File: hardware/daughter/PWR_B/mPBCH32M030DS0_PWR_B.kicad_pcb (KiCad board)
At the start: 2 copper layers, 66 x 66 mm, 76 parts, among them J1 B2B_PWR, J2 OUT0, J3 B2B_SIG, J4 OUT1, J5 OUT2, J6 OUT3, Q1 TKR74F04PB, Q2 TKR74F04PB, Q3 TKR74F04PB, Q4 TKR74F04PB, Q5 TKR74F04PB, Q6 TKR74F04PB, Q7 TKR74F04PB, Q8 TKR74F04PB

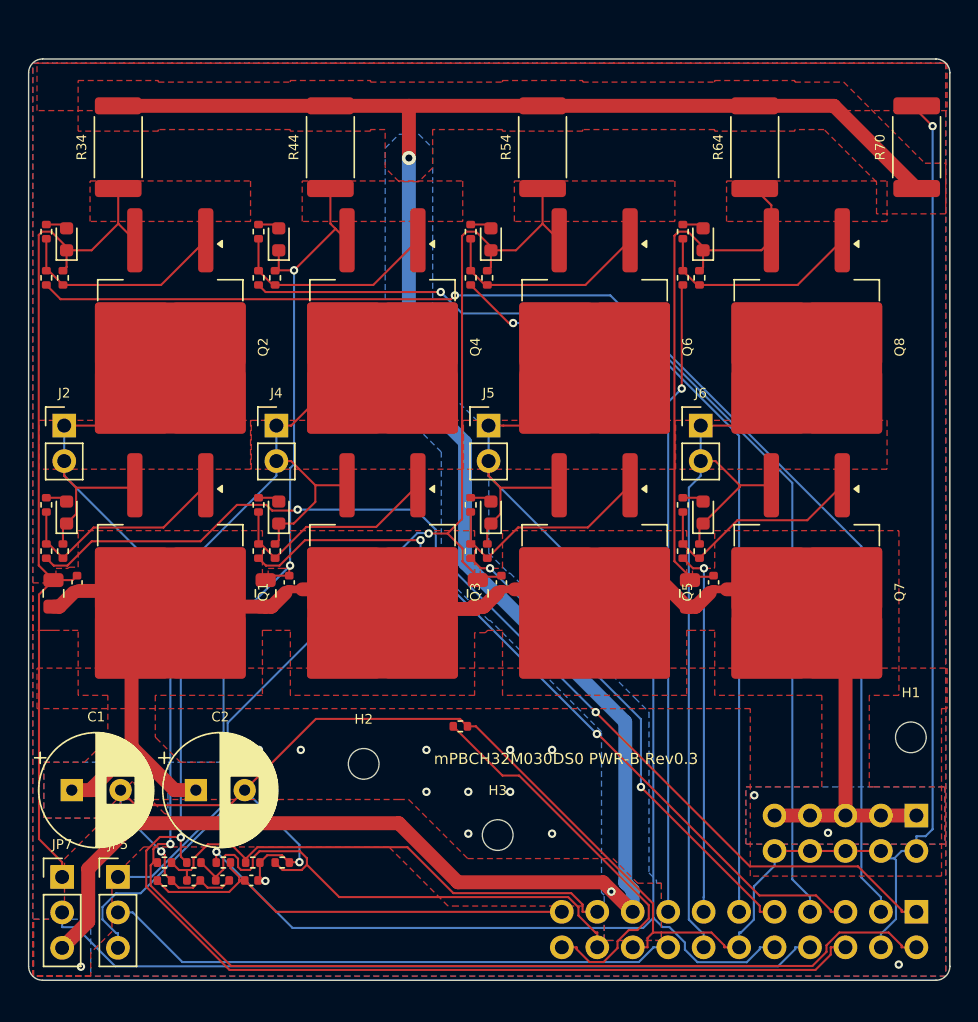
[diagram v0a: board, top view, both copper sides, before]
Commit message: Rev 0.4: DIP-42 MCU module + power boards A/B/C (KiCad 8)
- MCU module: 20.32 x 53.34mm (8 x 21 grid), DIP-42 (0.6in rows), fits
  an 82 x 52mm breadboard. Headers can be fitted from either side;
  signal names on bottom silk. All LEDs (power, status, 8 gate LEDs) on
  the module top.
- Power boards take the module in two 1x21 sockets (left/right
  symmetric mating). FETs/shunts on the heatsink side, no LEDs.
  Voltage-dependent parts (TVS, OVP divider, bulk caps, BEMF divider)
  moved to the power boards. Breakout board D removed.
  A/C: 20.32 x 71.94mm, B (TO-263 x8): 40.64 x 66.94mm.
- Capacitors re-selected for realistic size vs voltage/capacitance
  (4.7uF 1608, 10uF/25V 2012, 10uF/50V 1206, 4.7nF/100V 1608, low
  profile electrolytics).
- Schematics and boards generated in KiCad 8 format; netlists verified
  with KiCad 8.0.9.
- Layout pipeline: Freerouting bridge (parallel), second pass, early
  repair before pours, island-aware maze repair, DRC via kicad-cli.
- DRC: power boards A/B/C have 0 unconnected / 0 electrical errors.
  The MCU module still has unrouted connections (work in progress).

Co-Authored-By: Claude Opus 5.5 <noreply@anthropic.com>
Claude-Session: https://claude.ai/code/session_01LENFjjhDfYjJZV1NWhB9uV
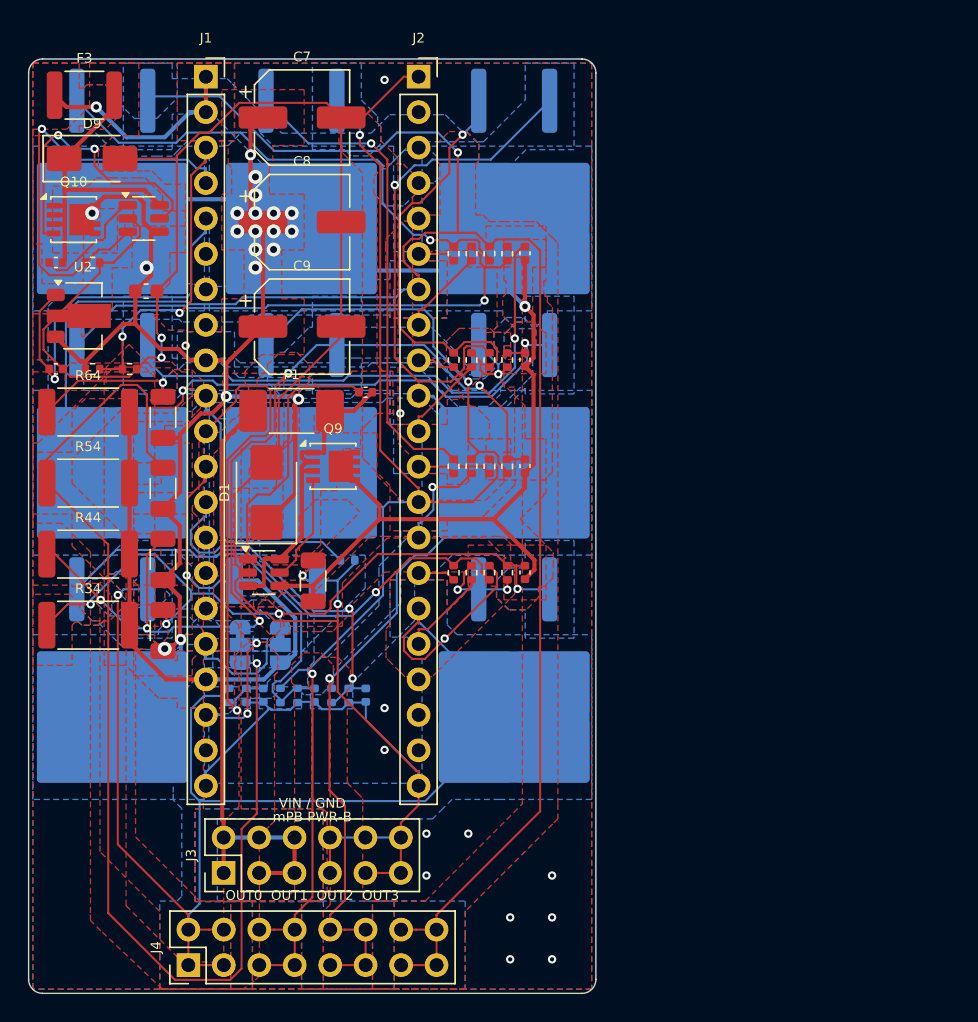
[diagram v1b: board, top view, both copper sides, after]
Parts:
- removed C2: 330uF/35V, CP_Radial_D8.0mm_P3.50mm
- removed D10: RED GH0, LED_0603_1608Metric
- removed D11: GREEN GL0, LED_0603_1608Metric
- removed D12: RED GH1, LED_0603_1608Metric
- removed D13: GREEN GL1, LED_0603_1608Metric
- removed D14: RED GH2, LED_0603_1608Metric
- removed D15: GREEN GL2, LED_0603_1608Metric
- removed D16: RED GH3, LED_0603_1608Metric
- removed D17: GREEN GL3, LED_0603_1608Metric
- removed H1, H2, H3: M2, MountingHole_2.2mm_M2
- removed J5: OUT2, PinHeader_1x02_P2.54mm_Vertical
- removed J6: OUT3, PinHeader_1x02_P2.54mm_Vertical
- removed R35, R36, R45, R46, R55, R56, R65, R66: 22k, R_0402_1005Metric
- added C3: 1uF/50V, C_0603_1608Metric, F.Cu at (8.41, 16.6)
- added C4: 1uF/25V, C_0402_1005Metric, F.Cu at (1.96, 22.2)
- added C5: 0.1uF/50V, C_0402_1005Metric, F.Cu at (24.1, 23.9)
- added C6: 0.1uF/50V, C_0402_1005Metric, F.Cu at (1.96, 14.6)
- added C7: 47uF/35V, CP_Elec_6.3x5.9, F.Cu at (19.6, 4.20)
- added C8: 47uF/35V, CP_Elec_6.3x5.9, F.Cu at (19.6, 11.7)
- added C9: 47uF/35V, CP_Elec_6.3x5.9, F.Cu at (19.6, 19.2)
- added D1: SMBJ24A, D_SMB, F.Cu at (17.0, 31.1)
- added D9: SMAJ20A, D_SMA, F.Cu at (4.54, 7.13)
- added F1: 10A, Fuse_Littelfuse_NANO2_2410, F.Cu at (18.8, 25.2)
- added F3: 5A, Fuse_1812_4532Metric, F.Cu at (4.00, 2.60)
- added Q10: TPN1R603PL, Vishay_PowerPAK_1212-8_Single, F.Cu at (3.23, 11.5)
- added Q9: TPN2R304PL, Vishay_PowerPAK_1212-8_Single, F.Cu at (21.8, 29.2)
- added R11: 180k 1%, R_0402_1005Metric, F.Cu at (4.58, 22.2)
- added R12: 10k 1%, R_0402_1005Metric, F.Cu at (7.23, 22.2)
- added R6: 100k, R_0402_1005Metric, F.Cu at (4.58, 14.6)
- added U2: 78L05, SOT-89-3, F.Cu at (3.90, 18.4)
- added U4: LM74700-Q1, SOT-23-6, F.Cu at (16.8, 36.8)
- added U5: LM74700-Q1, SOT-23-6, F.Cu at (8.24, 11.4)
- C1: value 330uF/35V -> 10uF/50V; footprint CP_Radial_D8.0mm_P3.50mm -> C_1206_3216Metric
- C31, C41, C51, C61: footprint C_0805_2012Metric -> C_1206_3216Metric
- C71, C72, C73, Q1, Q2, Q3, Q4, Q5, Q6, Q7, Q8, R70, R71, R72, R74, R75, R77, R78, TH1: moved to B.Cu
- J1: value B2B_PWR -> SOCK_L; footprint PinSocket_2x05_P2.54mm_Vertical -> PinSocket_1x21_P2.54mm_Vertical; moved to F.Cu
- J2: value OUT0 -> SOCK_R; footprint PinHeader_1x02_P2.54mm_Vertical -> PinSocket_1x21_P2.54mm_Vertical
- J3: value B2B_SIG -> PWR_IN; footprint PinSocket_2x11_P2.54mm_Vertical -> PinHeader_2x06_P2.54mm_Vertical; moved to F.Cu
- J4: value OUT1 -> MOTOR; footprint PinHeader_1x02_P2.54mm_Vertical -> PinHeader_2x08_P2.54mm_Vertical
- JP5, JP7: footprint PinHeader_1x03_P2.54mm_Vertical -> SolderJumper-3_P1.3mm_Bridged12_RoundedPad1.0x1.5mm_NumberLabels; moved to B.Cu
- moved J1 73.4 mm to (12.7, 1.27), turned to 0 degrees
- moved Q7 56.9 mm to (6.00, 10.6)
- moved R70 55.4 mm to (17.7, 37.4), turned to 0 degrees
- moved R64 51.4 mm to (4.26, 25.3), turned to 0 degrees
- moved Q8 50.3 mm to (6.00, 28.1)
- moved J3 49.7 mm to (14.0, 58.3)
- moved R54 40.5 mm to (4.26, 30.4), turned to 0 degrees
- moved C61 39.8 mm to (9.62, 25.7)
- moved J4 39.2 mm to (11.4, 64.9), turned to 90 degrees
- moved R33 38.2 mm to (34.3, 36.8)
- moved R32 37.1 mm to (31.7, 36.8)
- moved J2 35.6 mm to (27.9, 1.27)
- moved Q2 35.1 mm to (34.8, 45.6)
- moved R34 34.3 mm to (4.26, 40.6), turned to 0 degrees
- moved R44 33.9 mm to (4.26, 35.5), turned to 0 degrees
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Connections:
- J1 pad 1: VBUS -> USB_VBUS
- J1 pad 10: GND -> NTC
- J1 pad 2: GND -> USB_VBUS
- J1 pad 3: VBUS -> VBUS_SNS
- J1 pad 4: GND -> PD_PWR_EN
- J1 pad 5: VBUS -> +5V
- J1 pad 6: GND -> +3V3
- J1 pad 7: VBUS -> SWDIO
- J1 pad 8: GND -> nRST
- J2 pad 1: SW0 -> GND
- J2 pad 2: SW0 -> UART_TX
- J3 pad 1: HO0 -> VIN
- J3 pad 10: SW2 -> GND
- J3 pad 11: LO2 -> GND
- J3 pad 2: SW0 -> VIN
- J3 pad 3: LO0 -> VIN
- J3 pad 4: GND -> VIN
- J3 pad 5: HO1 -> VIN
- J3 pad 6: SW1 -> VIN
- J3 pad 7: LO1 -> GND
- J3 pad 8: ISA_SEL -> GND
- J3 pad 9: HO2 -> GND
- J4 pad 1: SW1 -> SW0
- J4 pad 2: SW1 -> SW0
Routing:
- net ISH: track 173.5 -> 38.3 mm, vias 3 -> 0
- net VBUS: track 138.0 -> 229.2 mm, vias 2 -> 22
- net LO0: track 93.1 -> 6.56 mm, vias 1 -> 0
- net SW3: track 69.4 -> 154.7 mm, vias 0 -> 1
- net HO0: track 77.5 -> 2.71 mm, vias 2 -> 0
- net LO1: track 75.4 -> 7.36 mm
- net HO1: track 54.9 -> 2.71 mm, vias 2 -> 0
- net LO2: track 57.8 -> 6.31 mm, vias 1 -> 0
- net ISA_SEL: track 56.4 -> 8.45 mm
- net VIN: track 0.00 -> 44.2 mm
- net LO3: track 45.3 -> 6.31 mm, vias 1 -> 0
- net SRC2: track 83.7 -> 120.3 mm, vias 1 -> 3
- net HO2: track 35.4 -> 2.71 mm, vias 2 -> 0
- net PD_PWR_EN: track 0.00 -> 31.7 mm, vias 0 -> 1
- net ISB_SEL: track 41.3 -> 9.76 mm, vias 0 -> 2
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- added copper zone on B.Cu, net SRC0
- added copper zone on B.Cu, net SRC1
- added copper zone on B.Cu, net SRC2
- added copper zone on B.Cu, net SRC3
- added copper zone on B.Cu, net SW0
- added copper zone on B.Cu, net SW1
- added copper zone on B.Cu, net SW2
- added copper zone on B.Cu, net SW3
- added copper zone on B.Cu, net USB_VBUS
- added copper zone on F.Cu, net USB_VBUS
- added copper zone on F.Cu, net USB_VBUS_P
- added copper zone on B.Cu, net VIN
- added copper zone on F.Cu, net VIN
- added copper zone on F.Cu, net VIN_F
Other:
- board size 66 x 66 mm -> 40.6 x 66.9 mm
- board text added: "OUT0 OUT1 OUT2 OUT3"
- board text added: "VIN / GND"
- board text added: "mPB PWR-B"
- board text removed: "mPBCH32M030DS0 PWR-B Rev0.3"

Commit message: Rev 0.4: rework module pinout for routability, power boards regenerated
- Module edge pin order follows the CH32M030 QFN48 pin sides so the
  breakout traces nest instead of crossing (J1: USB_VBUS, PD_PWR_EN,
  PC4/PC5, +3V3, +5V, SWDIO, VBUS, NTC, BEMF, HALL, ISx, TACH;
  J2: RX/TX, nRST, gate drive HO3..LO0, VBUS_SNS, I2C, nFAULT).
- Module: area under the QFN kept for fan-out (filters and the VHV/USB
  diode block moved away, gate LEDs right-aligned to J2).
- Power boards A/B/C re-placed for the new pinout (VBUS divider next to
  J2 VBUS_SNS, LM74700 next to its FET) and re-routed: all three at
  0 unconnected / 0 electrical DRC errors.
- Layout tooling: DRC via kicad-cli in a separate process, reload after
  SES import, selectable Freerouting jar, optional rip-up repair,
  configurable Freerouting timeout.
- MCU module still has unrouted connections (work in progress).

Co-Authored-By: Claude Opus 5.5 <noreply@anthropic.com>
Claude-Session: https://claude.ai/code/session_01LENFjjhDfYjJZV1NWhB9uV
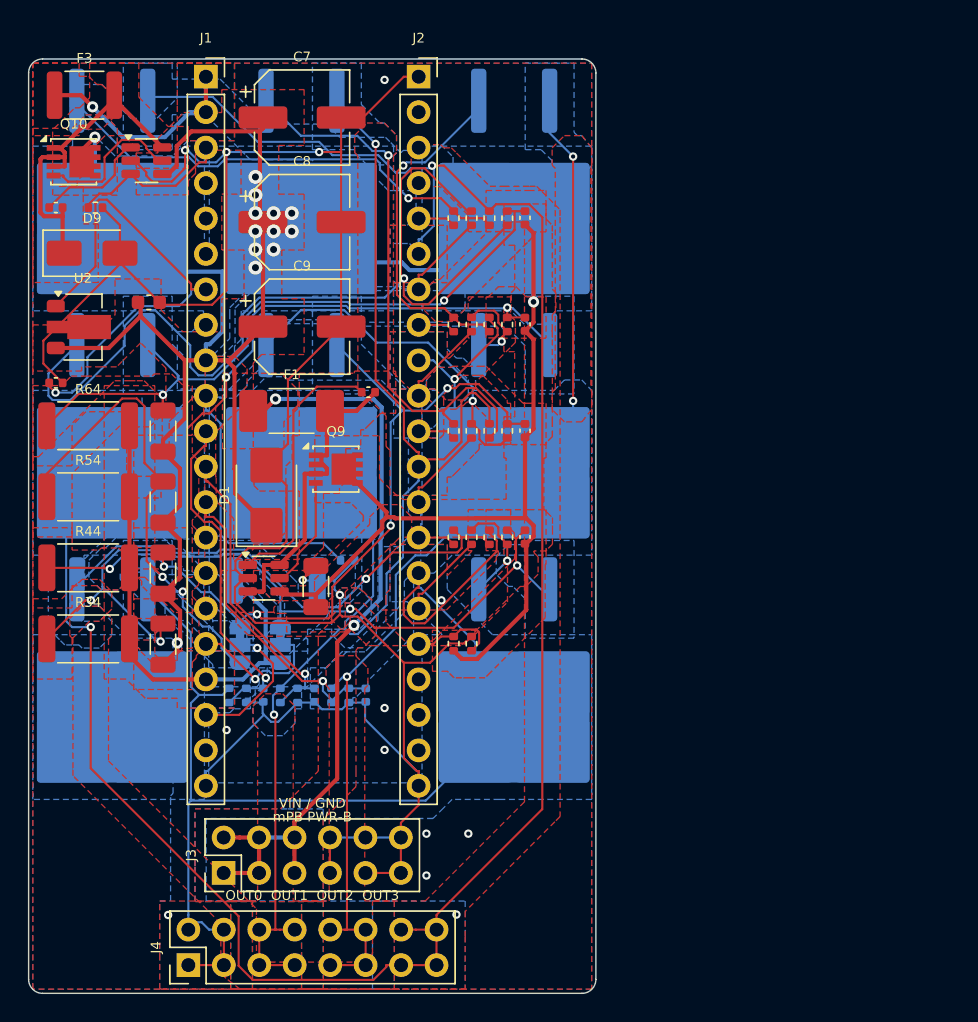
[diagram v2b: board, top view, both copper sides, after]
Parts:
- moved R11 32.5 mm to (30.4, 41.9), turned to 90 degrees
- moved R12 31.4 mm to (31.7, 41.9), turned to 90 degrees
- moved D9 6.78 mm to (4.54, 13.9)
- moved U5 4.14 mm to (8.45, 7.29)
- moved Q10 4.14 mm to (3.23, 7.37)
- moved R6 3.95 mm to (4.79, 10.7)
- moved C6 3.94 mm to (1.96, 10.6)
- moved C50 2.54 mm to (35.6, 19.0)
- moved R50 2.54 mm to (30.4, 19.0)
- moved R51 2.54 mm to (33.0, 19.0)
- moved R52 2.54 mm to (31.7, 19.0)
- moved R53 2.54 mm to (34.3, 19.0)
- moved C60 2.54 mm to (35.6, 11.4)
- moved R60 2.54 mm to (30.4, 11.4)
- moved R61 2.54 mm to (33.0, 11.4)
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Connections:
- J1 pad 3: VBUS_SNS -> PD_PWR_EN
- J1 pad 4: PD_PWR_EN -> GPIO_PC4
- J1 pad 5: +5V -> GPIO_PC5
- J1 pad 7: SWDIO -> +5V
- J1 pad 8: nRST -> SWDIO
- J2 pad 10: SW2 -> LO2
- J2 pad 11: LO2 -> HO1
- J2 pad 12: HO1 -> SW1
- J2 pad 13: SW1 -> LO1
- J2 pad 14: LO1 -> HO0
- J2 pad 15: HO0 -> SW0
- J2 pad 16: SW0 -> LO0
- J2 pad 17: LO0 -> VBUS_SNS
- J2 pad 18: I2C_SDA -> I2C_SCL
- J2 pad 19: I2C_SCL -> I2C_SDA
- J2 pad 2: UART_TX -> UART_RX
- J2 pad 3: UART_RX -> UART_TX
- J2 pad 4: GPIO_PC4 -> nRST
- J2 pad 5: GPIO_PC5 -> HO3
- J2 pad 6: HO3 -> SW3
- J2 pad 7: SW3 -> LO3
- J2 pad 8: LO3 -> HO2
- J2 pad 9: HO2 -> SW2
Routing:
- net SRC2: track 120.3 -> 80.9 mm, vias 3 -> 4
- net GL3: track 36.8 -> 65.7 mm
- net PD_PWR_EN: track 31.7 -> 11.7 mm, vias 1 -> 0
- net SW0: track 112.9 -> 96.6 mm
- net VBUS_SNS: track 22.0 -> 6.38 mm, vias 2 -> 0
- net SW3: track 154.7 -> 167.4 mm, vias 1 -> 3
- net VBUS: track 229.2 -> 241.6 mm, vias 22 -> 14
- net VIN: track 44.2 -> 55.9 mm, vias 0 -> 2
- net BEMF_U: track 35.2 -> 24.4 mm
- net Q10_G: track 20.9 -> 10.9 mm, vias 2 -> 0
- net SRC1: track 69.0 -> 59.5 mm
- net BEMF_V: track 31.1 -> 22.0 mm
- net SW1: track 102.6 -> 110.6 mm
- net SRC0: track 49.8 -> 57.5 mm
- net +5V: track 27.7 -> 35.2 mm
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
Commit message: 9マス版に一本化 (8マス版を削除)
- 8 マス版 (20.32mm) は JLCPCB の 2 層標準 0.127mm で配線しきれないため削除
- 9 マス版 (22.86mm, 端子列 0.7in) を hardware/ 直下・hardware/daughter/・hardware/fab/・docs/pcb/ へ移動
- ベタなし版は hardware/nopour/ (図は docs/pcb/nopour/)
- gen_pcb.py から MPB_W9 の切り替えを外し 9 マス固定に。既定ルールは 0.127mm / ビア 0.6/0.3
  (再生成した配置が確定済みの 4 基板と一致することを確認)
- 回路図の注記 (外形・列間) を 22.86mm / 17.78mm に更新し PDF を再出力
- README / stacking.md / design.md を 9 マス版のみの記述に更新

Co-Authored-By: Claude Opus 5.5 <noreply@anthropic.com>
Claude-Session: https://claude.ai/code/session_01LENFjjhDfYjJZV1NWhB9uV
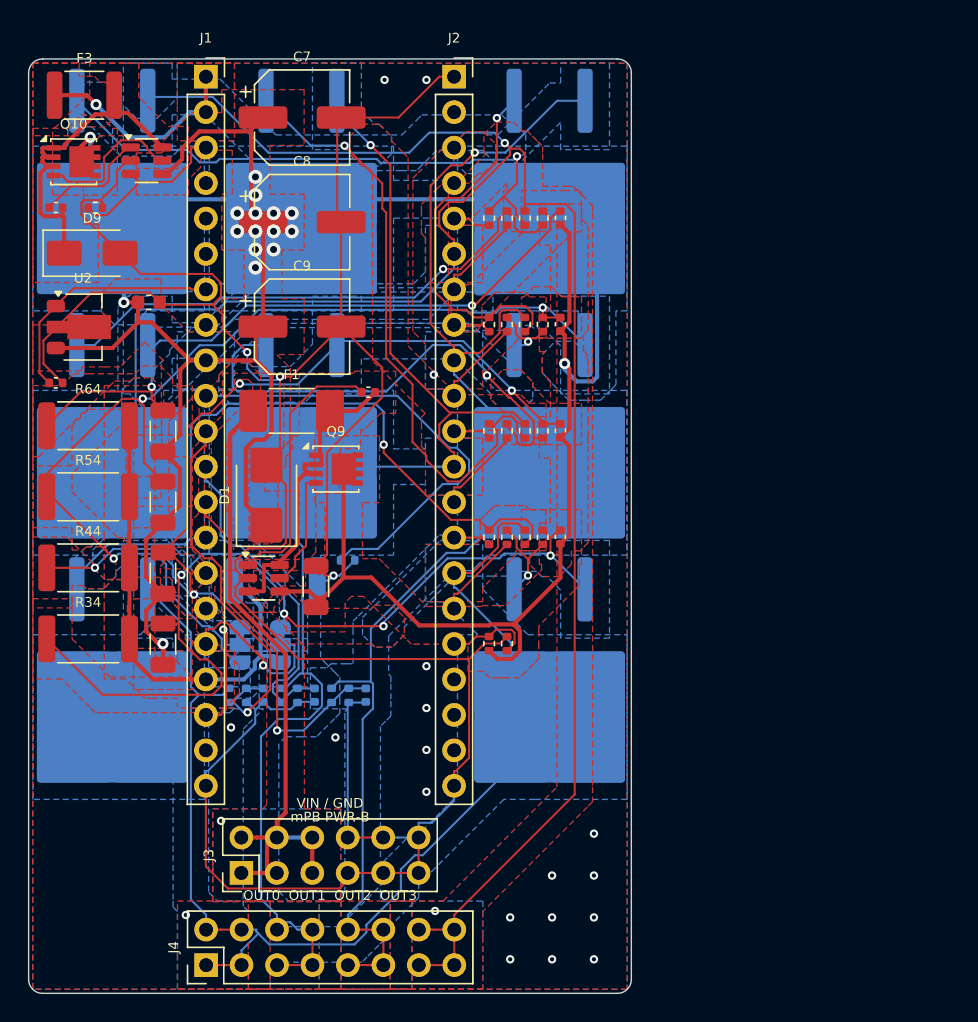
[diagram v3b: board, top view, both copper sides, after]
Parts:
- moved R31 2.54 mm to (35.5, 34.3)
- moved R41 2.54 mm to (35.5, 26.6)
- moved R51 2.54 mm to (35.5, 19.0)
- moved R61 2.54 mm to (35.5, 11.4)
- moved Q2 2.54 mm to (37.3, 45.6)
- moved Q5 2.54 mm to (37.3, 10.6)
- moved Q6 2.54 mm to (37.3, 28.1)
- moved R11 2.54 mm to (33.0, 41.9)
- moved R12 2.54 mm to (34.3, 41.9)
- moved R30 2.54 mm to (33.0, 34.3)
- moved R32 2.54 mm to (34.3, 34.3)
- moved R40 2.54 mm to (33.0, 26.6)
- moved R42 2.54 mm to (34.3, 26.6)
- moved R50 2.54 mm to (33.0, 19.0)
- moved R52 2.54 mm to (34.3, 19.0)
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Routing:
- net GND: track 181.1 -> 213.3 mm, vias 12 -> 20
- net GL3: track 65.7 -> 39.0 mm
- net +5V: track 35.2 -> 17.6 mm, vias 1 -> 0
- net GH0: track 36.5 -> 51.0 mm
- net NTC: track 19.8 -> 33.5 mm
- net VBUS: track 241.6 -> 253.3 mm, vias 14 -> 17
- net GL1: track 24.5 -> 35.5 mm
- net VIN: track 55.9 -> 45.9 mm, vias 2 -> 1
- net SRC0: track 57.5 -> 65.1 mm
- net SW3: track 167.4 -> 160.3 mm, vias 3 -> 2
- net GH3: track 34.1 -> 41.2 mm
- net SW1: track 110.6 -> 104.9 mm, vias 2 -> 1
- net SRC2: track 80.9 -> 75.7 mm, vias 4 -> 3
- net SW2: track 97.6 -> 102.7 mm, vias 4 -> 2
- net BEMF_W: track 22.1 -> 26.2 mm
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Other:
- board size 40.6 x 66.9 mm -> 43.2 x 66.9 mm
